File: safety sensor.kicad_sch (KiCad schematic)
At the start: 29 parts, among them IC1 STM8S003F3P6, J1 Conn_01x02, J2 SDA, J3 SCL, J4 INT, J5 Conn_01x02, J6 SWIM, U1 LD1117V33, U2 VCNL3020-GS08

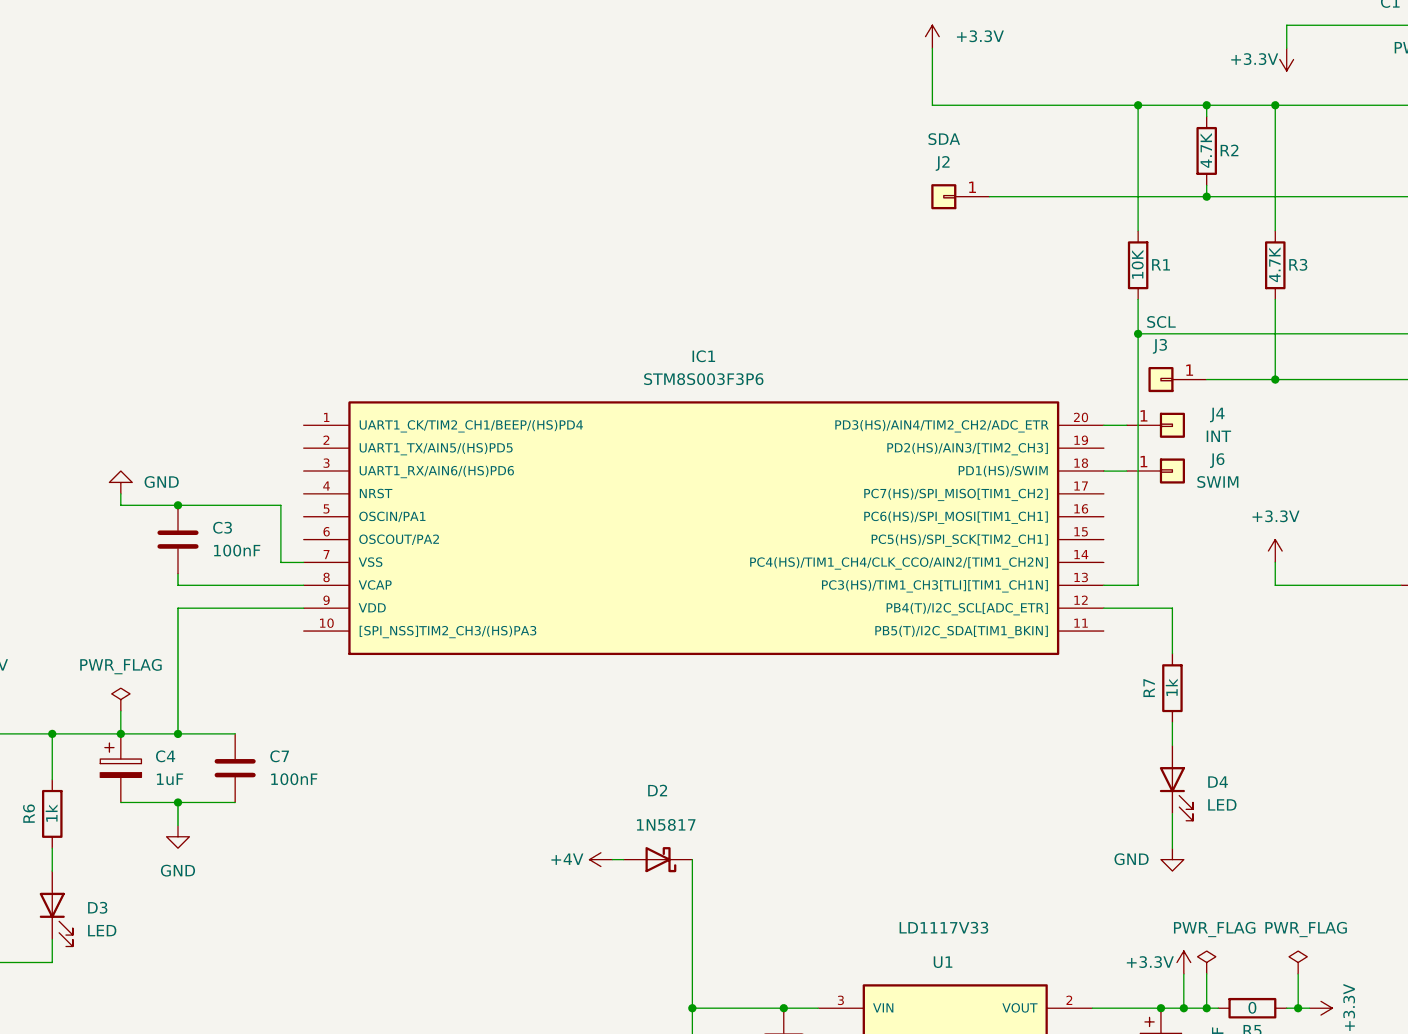
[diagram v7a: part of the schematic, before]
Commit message: flip stm8 side
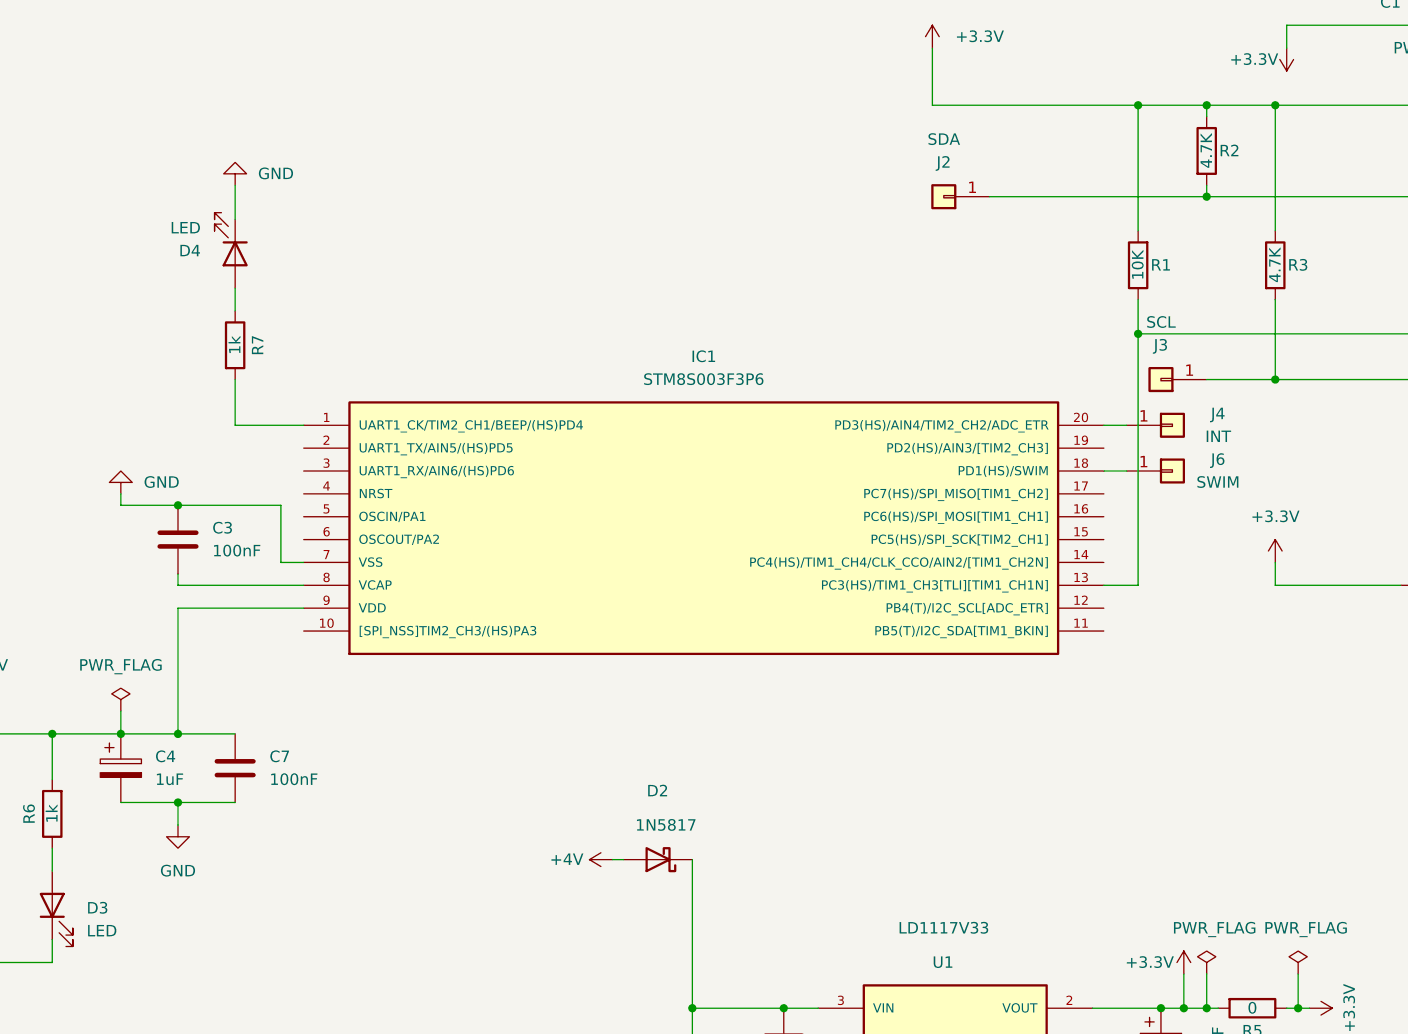
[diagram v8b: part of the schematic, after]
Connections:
- net at IC1.1 (UART1_CK/TIM2_CH1/BEEP/(HS)PD4): now also R7.2
- net at IC1.12 (PB4(T)/I2C_SCL[ADC_ETR]): no longer R7.2
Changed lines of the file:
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@@
-    (stroke (width 0) (type default) (color 0 0 0 0))
-  )
-  (wire (pts (xy 157.48 114.3) (xy 157.48 116.84))
     (stroke (width 0) (type default) (color 0 0 0 0))
   )
@@
     (stroke (width 0) (type default) (color 0 0 0 0))
   )
+  (wire (pts (xy 53.34 54.61) (xy 53.34 58.42))
+    (stroke (width 0) (type default) (color 0 0 0 0))
+  )
   (wire (pts (xy 130.81 162.56) (xy 148.59 162.56))
     (stroke (width 0) (type default) (color 0 0 0 0))
@@
     (stroke (width 0) (type default) (color 0 0 0 0))
   )
+  (wire (pts (xy 53.34 76.2) (xy 53.34 81.28))
+    (stroke (width 0) (type default) (color 0 0 0 0))
+  )
   (wire (pts (xy 170.18 146.05) (xy 171.45 146.05))
     (stroke (width 0) (type default) (color 0 0 0 0))
@@
     (stroke (width 0) (type default) (color 0 0 0 0))
   )
+  (wire (pts (xy 60.96 81.28) (xy 53.34 81.28))
+    (stroke (width 0) (type default) (color 0 0 0 0))
+  )
   (wire (pts (xy 33.02 115.57) (xy 33.02 120.65))
     (stroke (width 0) (type default) (color 0 0 0 0))
   )
-  (wire (pts (xy 149.86 101.6) (xy 157.48 101.6))
-    (stroke (width 0) (type default) (color 0 0 0 0))
-  )
   (wire (pts (xy 40.64 115.57) (xy 46.99 115.57))
     (stroke (width 0) (type default) (color 0 0 0 0))
@@
     (stroke (width 0) (type default) (color 0 0 0 0))
   )
+  (wire (pts (xy 53.34 68.58) (xy 53.34 66.04))
+    (stroke (width 0) (type default) (color 0 0 0 0))
+  )
   (wire (pts (xy 195.58 99.06) (xy 203.2 99.06))
     (stroke (width 0) (type default) (color 0 0 0 0))
@@
     (stroke (width 0) (type default) (color 0 0 0 0))
   )
-  (wire (pts (xy 157.48 128.27) (xy 157.48 124.46))
-    (stroke (width 0) (type default) (color 0 0 0 0))
-  )
   (wire (pts (xy 149.86 99.06) (xy 153.67 99.06))
     (stroke (width 0) (type default) (color 0 0 0 0))
@@
   )
   (wire (pts (xy 185.42 66.04) (xy 200.66 66.04))
-    (stroke (width 0) (type default) (color 0 0 0 0))
-  )
-  (wire (pts (xy 157.48 106.68) (xy 157.48 101.6))
     (stroke (width 0) (type default) (color 0 0 0 0))
   )
@@
     (pin "1")
   )
+  (symbol (lib_id "Device:LED") (at 53.34 62.23 270) (unit 1)
+    (in_bom yes) (on_board yes) (fields_autoplaced)
+    (property "Reference" "D4" (id 0) (at 49.53 61.9126 90)
+      (effects (font (size 1.27 1.27)) (justify right))
+    )
+    (property "Value" "LED" (id 1) (at 49.53 59.3726 90)
+      (effects (font (size 1.27 1.27)) (justify right))
+    )
+    (property "Footprint" "LED_THT:LED_D5.0mm" (id 2) (at 53.34 62.23 0)
+      (effects (font (size 1.27 1.27)) hide)
+    )
+    (property "Datasheet" "~" (id 3) (at 53.34 62.23 0)
+      (effects (font (size 1.27 1.27)) hide)
+    )
+    (pin "1")
+    (pin "2")
+  )
   (symbol (lib_id "Device:R") (at 186.69 99.06 90) (unit 1)
     (in_bom yes) (on_board yes)
@@
     (pin "1")
   )
-  (symbol (lib_id "Device:LED") (at 157.48 120.65 90) (unit 1)
-    (in_bom yes) (on_board yes) (fields_autoplaced)
-    (property "Reference" "D4" (id 0) (at 161.29 120.9674 90)
-      (effects (font (size 1.27 1.27)) (justify right))
-    )
-    (property "Value" "LED" (id 1) (at 161.29 123.5074 90)
-      (effects (font (size 1.27 1.27)) (justify right))
-    )
-    (property "Footprint" "LED_THT:LED_D5.0mm" (id 2) (at 157.48 120.65 0)
-      (effects (font (size 1.27 1.27)) hide)
-    )
-    (property "Datasheet" "~" (id 3) (at 157.48 120.65 0)
-      (effects (font (size 1.27 1.27)) hide)
-    )
-    (pin "1")
-    (pin "2")
-  )
   (symbol (lib_id "power:PWR_FLAG") (at 195.58 96.52 0) (unit 1)
     (in_bom yes) (on_board yes) (fields_autoplaced)
@@
     )
     (property "Datasheet" "" (id 3) (at 158.75 142.24 0)
+      (effects (font (size 1.27 1.27)) hide)
+    )
+    (pin "1")
+  )
+  (symbol (lib_id "power:GND") (at 53.34 54.61 180) (unit 1)
+    (in_bom yes) (on_board yes) (fields_autoplaced)
+    (property "Reference" "#PWR0118" (id 0) (at 53.34 48.26 0)
+      (effects (font (size 1.27 1.27)) hide)
+    )
+    (property "Value" "GND" (id 1) (at 55.88 53.3399 0)
+      (effects (font (size 1.27 1.27)) (justify right))
+    )
+    (property "Footprint" "" (id 2) (at 53.34 54.61 0)
+      (effects (font (size 1.27 1.27)) hide)
+    )
+    (property "Datasheet" "" (id 3) (at 53.34 54.61 0)
       (effects (font (size 1.27 1.27)) hide)
     )
@@
     (pin "1")
     (pin "2")
-  )
-  (symbol (lib_id "power:GND") (at 157.48 128.27 0) (unit 1)
-    (in_bom yes) (on_board yes) (fields_autoplaced)
-    (property "Reference" "#PWR0118" (id 0) (at 157.48 134.62 0)
-      (effects (font (size 1.27 1.27)) hide)
-    )
-    (property "Value" "GND" (id 1) (at 154.94 129.5401 0)
-      (effects (font (size 1.27 1.27)) (justify right))
-    )
-    (property "Footprint" "" (id 2) (at 157.48 128.27 0)
-      (effects (font (size 1.27 1.27)) hide)
-    )
-    (property "Datasheet" "" (id 3) (at 157.48 128.27 0)
-      (effects (font (size 1.27 1.27)) hide)
-    )
-    (pin "1")
   )
   (symbol (lib_id "Device:R") (at 33.02 124.46 180) (unit 1)
@@
     (pin "1")
   )
+  (symbol (lib_id "Device:R") (at 53.34 72.39 0) (unit 1)
+    (in_bom yes) (on_board yes)
+    (property "Reference" "R7" (id 0) (at 55.88 72.39 90))
+    (property "Value" "1k" (id 1) (at 53.34 72.39 90))
+    (property "Footprint" "Resistor_THT:R_Axial_DIN0207_L6.3mm_D2.5mm_P10.16mm_Horizontal" (id 2) (at 51.562 72.39 90)
+      (effects (font (size 1.27 1.27)) hide)
+    )
+    (property "Datasheet" "~" (id 3) (at 53.34 72.39 0)
+      (effects (font (size 1.27 1.27)) hide)
+    )
+    (pin "1")
+    (pin "2")
+  )
   (symbol (lib_id "power:+4V") (at 35.56 176.53 270) (unit 1)
     (in_bom yes) (on_board yes) (fields_autoplaced)
@@
     )
     (pin "1")
-  )
-  (symbol (lib_id "Device:R") (at 157.48 110.49 180) (unit 1)
-    (in_bom yes) (on_board yes)
-    (property "Reference" "R7" (id 0) (at 154.94 110.49 90))
-    (property "Value" "1k" (id 1) (at 157.48 110.49 90))
-    (property "Footprint" "Resistor_THT:R_Axial_DIN0207_L6.3mm_D2.5mm_P10.16mm_Horizontal" (id 2) (at 159.258 110.49 90)
-      (effects (font (size 1.27 1.27)) hide)
-    )
-    (property "Datasheet" "~" (id 3) (at 157.48 110.49 0)
-      (effects (font (size 1.27 1.27)) hide)
-    )
-    (pin "1")
-    (pin "2")
   )
   (symbol (lib_id "power:PWR_FLAG") (at 171.45 142.24 0) (unit 1)
@@
       (reference "#PWR0117") (unit 1) (value "+4V") (footprint "")
     )
-    (path "/7997639c-d6b3-4967-bf66-d71db525babf"
+    (path "/4325ebc9-edf0-4993-9b90-19201ccc814f"
       (reference "#PWR0118") (unit 1) (value "GND") (footprint "")
     )
@@
       (reference "D3") (unit 1) (value "LED") (footprint "LED_THT:LED_D5.0mm")
     )
-    (path "/1c7882b5-7f41-46c5-865a-215e26b59025"
+    (path "/0f08df69-205a-4480-963e-6720127fcd23"
       (reference "D4") (unit 1) (value "LED") (footprint "LED_THT:LED_D5.0mm")
     )
@@
       (reference "R6") (unit 1) (value "1k") (footprint "Resistor_THT:R_Axial_DIN0207_L6.3mm_D2.5mm_P10.16mm_Horizontal")
     )
-    (path "/e7f5e550-f264-4e87-aa56-0484c1e9d730"
+    (path "/d7ecd415-fdfc-4feb-b807-a29cf0e95407"
       (reference "R7") (unit 1) (value "1k") (footprint "Resistor_THT:R_Axial_DIN0207_L6.3mm_D2.5mm_P10.16mm_Horizontal")
     )
